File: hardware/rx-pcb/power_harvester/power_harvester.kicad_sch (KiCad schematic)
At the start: 30 parts, among them J1 Conn_Coaxial_Small, J2 Conn_01x02_Pin

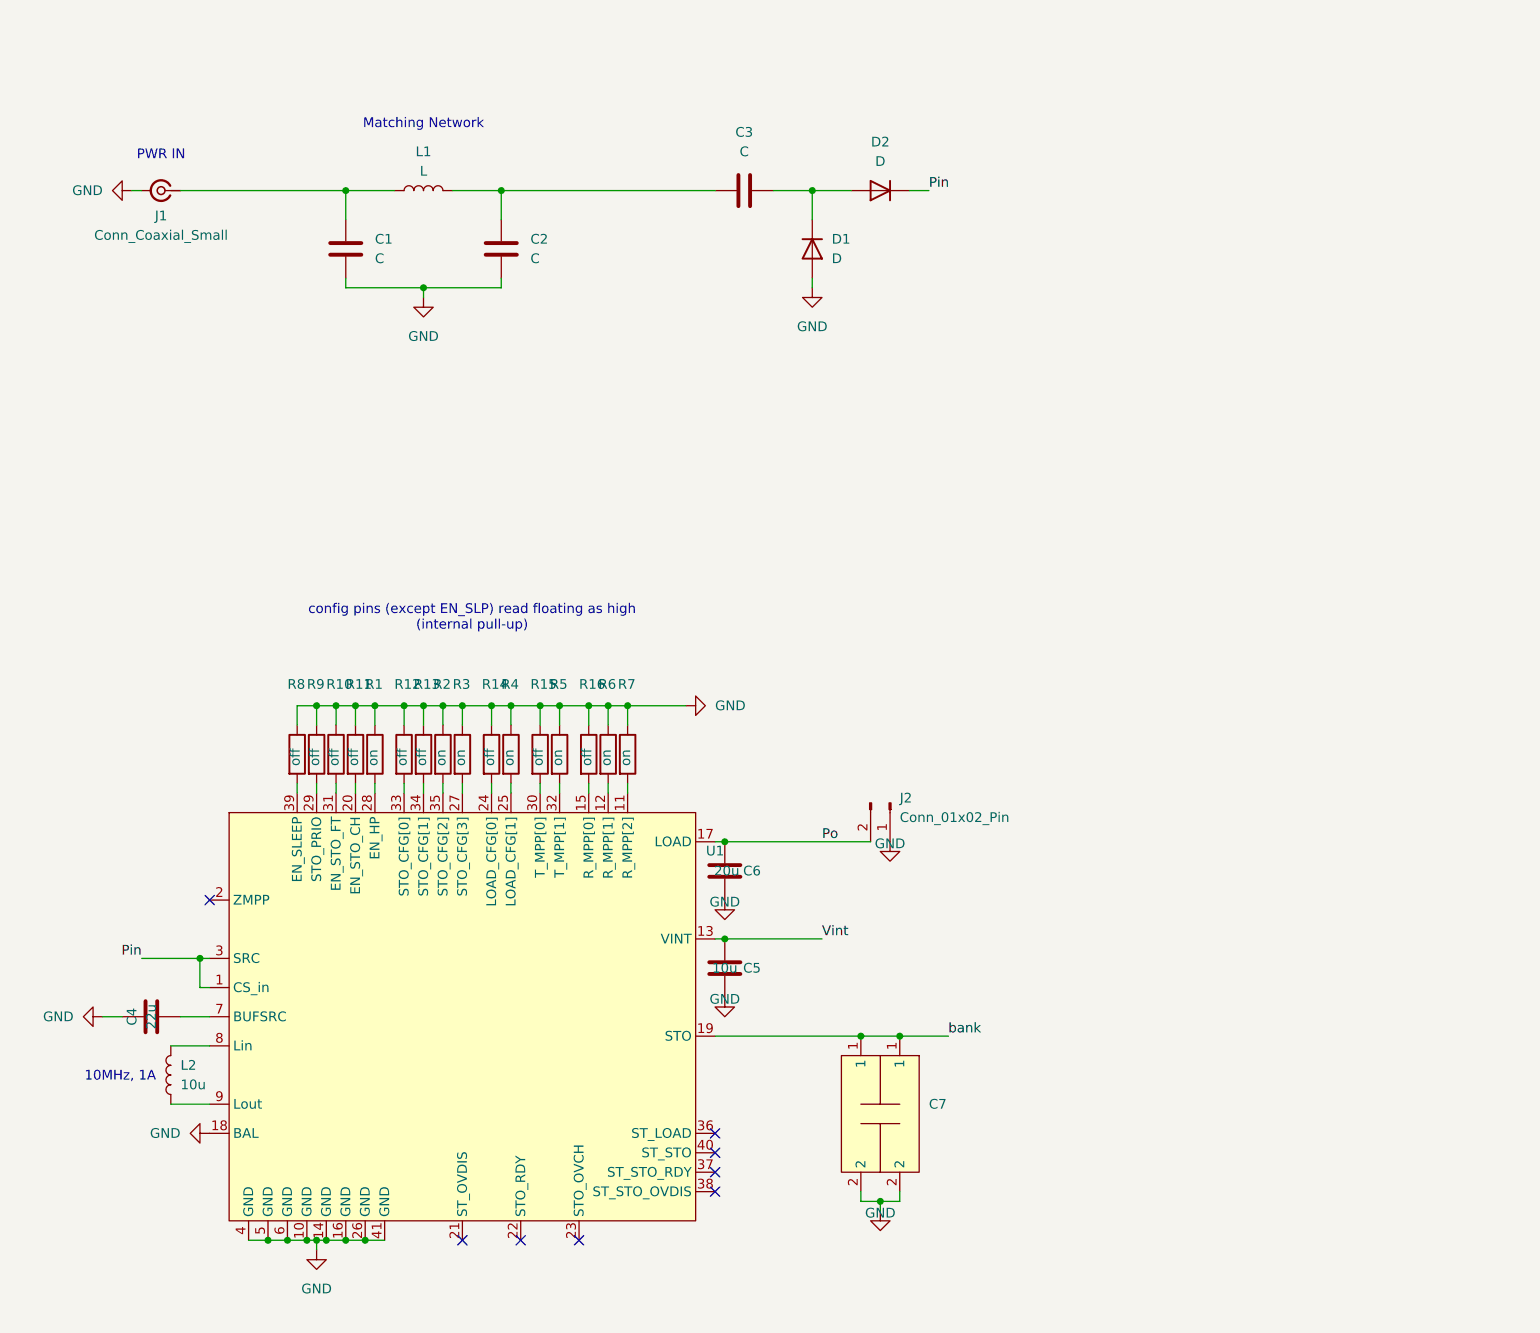
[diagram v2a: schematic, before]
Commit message: updated harvester PCB with reverse voltage suppression diodes.
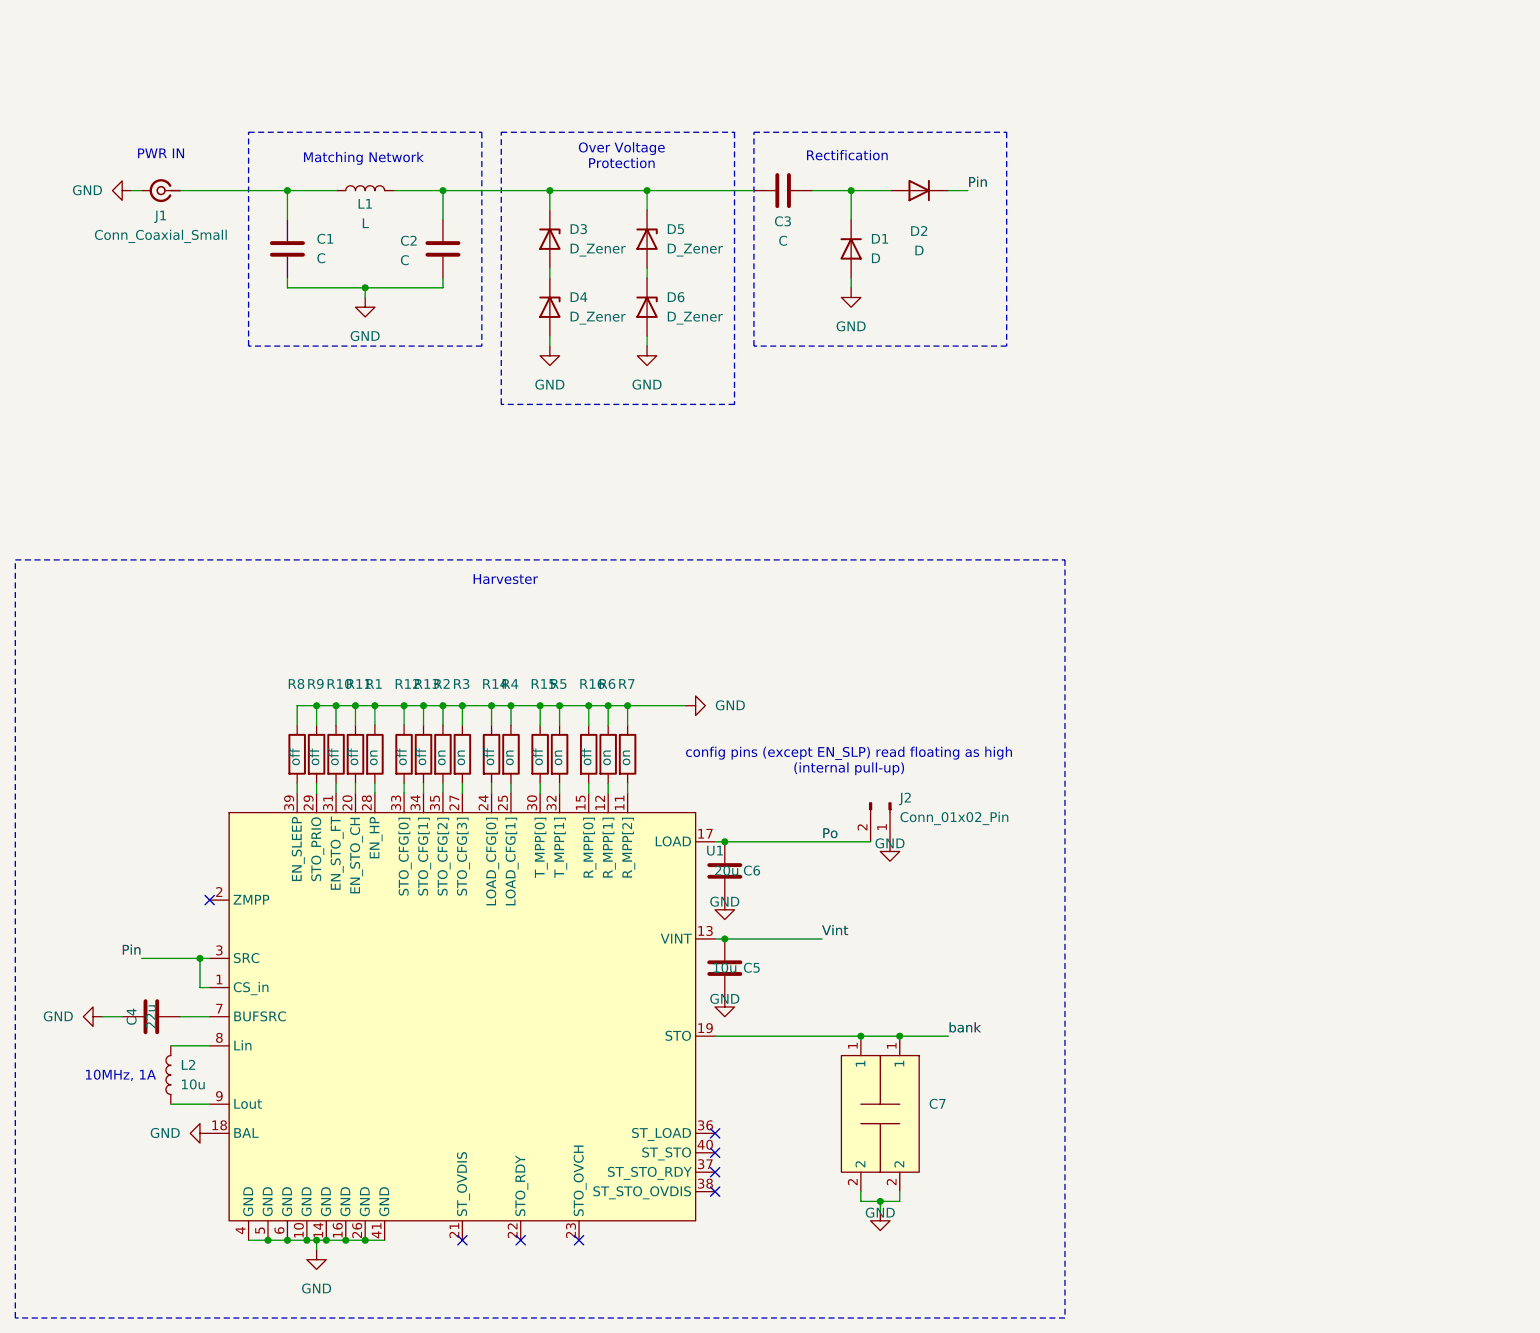
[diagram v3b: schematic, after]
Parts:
- added D3, D4, D5, D6: D_Zener, Capacitor_SMD:C_0201_0603Metric, symbol Device:D_Zener
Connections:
- net GND: now also D4.2 (A), D6.2 (A)
- net at C2.1, C3.1, L1.2: now also D3.1 (K), D5.1 (K)
- new net: D5.2 (A), D6.1 (K)
- new net: D3.2 (A), D4.1 (K)
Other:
- note added: "Harvester"
- note added: "Over Voltage Protection"
- note added: "Rectification"
- moved on the sheet: C1, C2, C3, D1, D2, L1

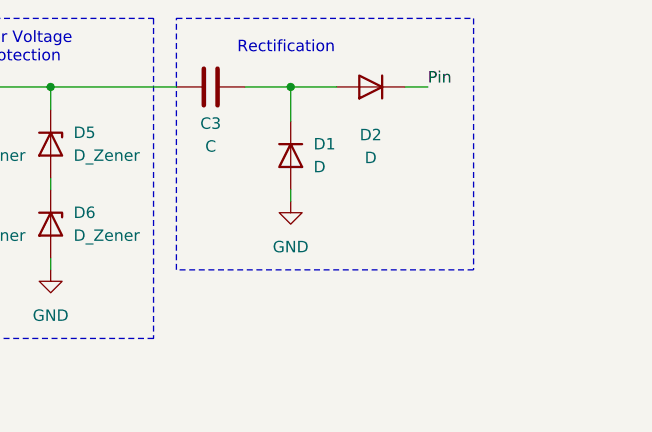
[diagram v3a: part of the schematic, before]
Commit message: updated harvester with compartmentalization testing resistors and test points. updated bluetooth test to use a low Vf diode rather than an LED for reverse current protection. must update footprint for that.
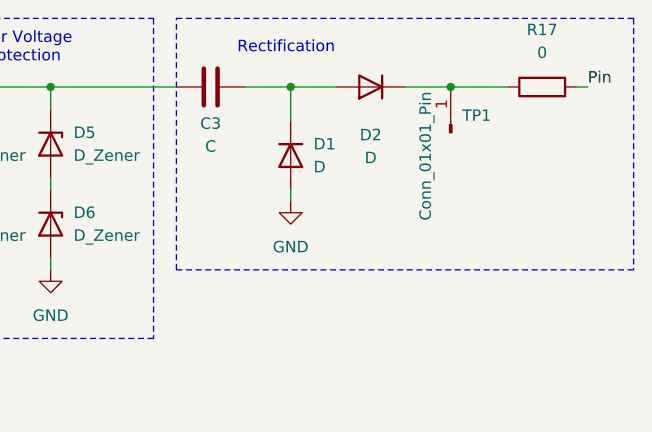
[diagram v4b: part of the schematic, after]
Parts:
- added R17: 0, Resistor_SMD:R_0201_0603Metric_Pad0.64x0.40mm_HandSolder, symbol Device:R
- added TP1: Conn_01x01_Pin, Connector_PinHeader_2.54mm:PinHeader_1x01_P2.54mm_Vertical, symbol Connector:Conn_01x01_Pin
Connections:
- net Pin: now also R17.2; no longer D2.1 (K)
- new net: D2.1 (K), R17.1, TP1.1 (Pin_1)
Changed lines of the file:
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@@
 	(rectangle
 		(start 109.22 38.1)
-		(end 142.24 66.04)
+		(end 160.02 66.04)
 		(stroke
 			(width 0)
@@
 		(color 0 0 0 0)
 	)
+	(junction
+		(at 139.7 45.72)
+		(diameter 0)
+		(color 0 0 0 0)
+	)
 	(no_connect
 		(at 86.36 182.88)
@@
 	(wire
 		(pts
+			(xy 134.62 45.72) (xy 139.7 45.72)
+		)
+		(stroke
+			(width 0)
+			(type default)
+		)
+	)
+	(wire
+		(pts
 			(xy 121.92 45.72) (xy 121.92 49.53)
 		)
@@
 	(wire
 		(pts
-			(xy 137.16 45.72) (xy 134.62 45.72)
+			(xy 146.05 45.72) (xy 139.7 45.72)
+		)
+		(stroke
+			(width 0)
+			(type default)
+		)
+	)
+	(wire
+		(pts
+			(xy 153.67 45.72) (xy 154.94 45.72)
 		)
 		(stroke
@@
 	)
 	(label "Pin"
-		(at 137.16 45.72 0)
+		(at 154.94 45.72 0)
 		(effects
 			(font
@@
 	)
 	(symbol
+		(lib_id "Device:R")
+		(at 149.86 45.72 90)
+		(unit 1)
+		(exclude_from_sim no)
+		(in_bom yes)
+		(on_board yes)
+		(dnp no)
+		(fields_autoplaced yes)
+		(property "Reference" "R17"
+			(at 149.86 39.37 90)
+			(effects
+				(font
+					(size 1.27 1.27)
+				)
+			)
+		)
+		(property "Value" "0"
+			(at 149.86 41.91 90)
+			(effects
+				(font
+					(size 1.27 1.27)
+				)
+			)
+		)
+		(property "Footprint" "Resistor_SMD:R_0201_0603Metric_Pad0.64x0.40mm_HandSolder"
+			(at 149.86 47.498 90)
+			(effects
+				(font
+					(size 1.27 1.27)
+				)
+				(hide yes)
+			)
+		)
+		(property "Datasheet" "~"
+			(at 149.86 45.72 0)
+			(effects
+				(font
+					(size 1.27 1.27)
+				)
+				(hide yes)
+			)
+		)
+		(property "Description" "Resistor"
+			(at 149.86 45.72 0)
+			(effects
+				(font
+					(size 1.27 1.27)
+				)
+				(hide yes)
+			)
+		)
+		(pin "1"
+		)
+		(pin "2"
+		)
+		(instances
+			(project ""
+				(path "/5e0abde9-f038-4a18-8052-8202be093003"
+					(reference "R17")
+					(unit 1)
+				)
+			)
+		)
+	)
+	(symbol
 		(lib_id "Connector:Conn_01x02_Pin")
 		(at 127 125.73 270)
@@
 					(unit 1)
 				)
+			)
+		)
+	)
+	(symbol
+		(lib_id "Connector:Conn_01x01_Pin")
+		(at 139.7 50.8 90)
+		(unit 1)
+		(exclude_from_sim no)
+		(in_bom yes)
+		(on_board yes)
+		(dnp no)
+		(property "Reference" "TP1"
+			(at 140.97 48.8949 90)
+			(effects
+				(font
+					(size 1.27 1.27)
+				)
+				(justify right)
+			)
+		)
+		(property "Value" "Conn_01x01_Pin"
+			(at 136.906 46.228 0)
+			(effects
+				(font
+					(size 1.27 1.27)
+				)
+				(justify right)
+			)
+		)
+		(property "Footprint" "Connector_PinHeader_2.54mm:PinHeader_1x01_P2.54mm_Vertical"
+			(at 139.7 50.8 0)
+			(effects
+				(font
+					(size 1.27 1.27)
+				)
+				(hide yes)
+			)
+		)
+		(property "Datasheet" "~"
+			(at 139.7 50.8 0)
+			(effects
+				(font
+					(size 1.27 1.27)
+				)
+				(hide yes)
+			)
+		)
+		(property "Description" "Generic connector, single row, 01x01, script generated"
+			(at 139.7 50.8 0)
+			(effects
+				(font
+					(size 1.27 1.27)
+				)
+				(hide yes)
+			)
+		)
+		(pin "1"
+		)
+		(instances
+			(project ""
+				(path "/5e0abde9-f038-4a18-8052-8202be093003"
+					(reference "TP1")
+					(unit 1)
+				)

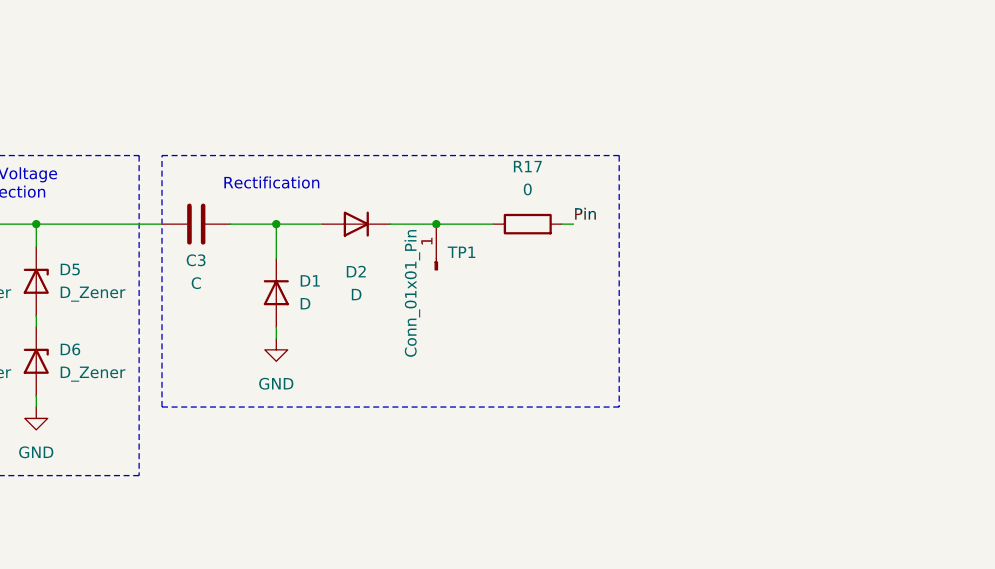
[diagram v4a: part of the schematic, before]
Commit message: simulation and cleaning
actually simulated my stupid 5k impedance match idea, it sucked because my rectifier is a 400 ohm impedance to ground. cleaning up the github.
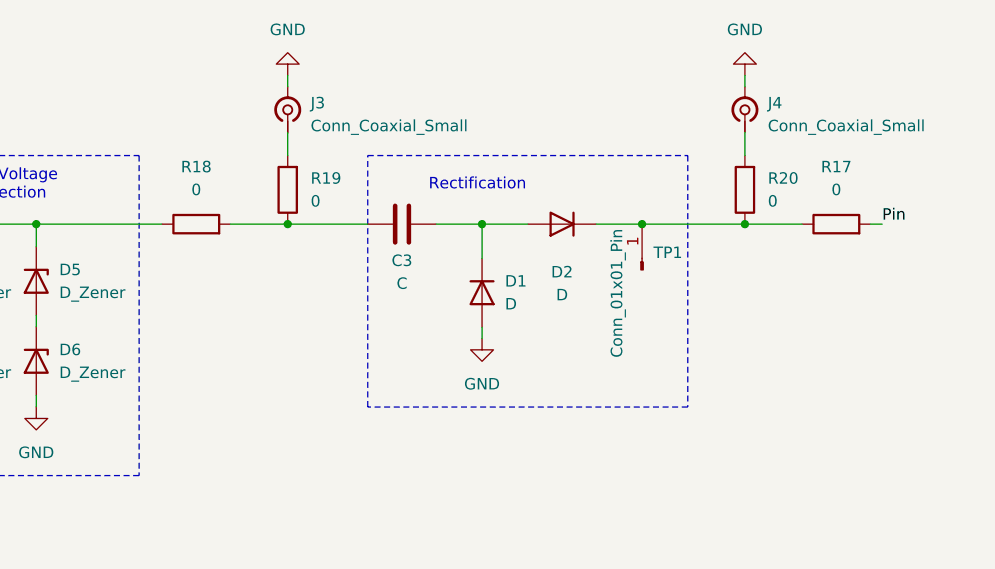
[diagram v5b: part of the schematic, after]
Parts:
- added J3, J4: Conn_Coaxial_Small, symbol Connector:Conn_Coaxial_Small
- added R18, R19, R20: 0, Resistor_SMD:R_0201_0603Metric_Pad0.64x0.40mm_HandSolder, symbol Device:R
- C7, U1: value ~ -> (none)
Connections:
- net GND: now also J3.2 (Ext), J4.2 (Ext)
- net at C2.1, D3.1 (K), D5.1 (K)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: now also R18.1; no longer C3.1
- net at D2.1 (K), R17.1, TP1.1 (Pin_1): now also R20.1
- new net: C3.1, R18.2, R19.1
- new net: J3.1 (In), R19.2
- new net: J4.1 (In), R20.2
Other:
- moved on the sheet: C3, D1, D2, R17, TP1

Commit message: power harvester updates and cleanup
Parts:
- removed D5, D6: D_Zener, Capacitor_SMD:C_0201_0603Metric, symbol Device:D_Zener
- removed TP1: Conn_01x01_Pin, Connector_PinHeader_2.54mm:PinHeader_1x01_P2.54mm_Vertical, symbol Connector:Conn_01x01_Pin
- added C10, C9: C, Capacitor_SMD:C_0603_1608Metric_Pad1.08x0.95mm_HandSolder, symbol Device:C
- added C8: 22u, Capacitor_SMD:C_0603_1608Metric_Pad1.08x0.95mm_HandSolder, symbol Device:C
- added L3: L, Inductor_SMD:L_0805_2012Metric_Pad1.05x1.20mm_HandSolder, symbol Device:L
- C1, C2, C4, C5, C6: footprint Capacitor_SMD:C_0805_2012Metric_Pad1.18x1.45mm_HandSolder -> Capacitor_SMD:C_0603_1608Metric_Pad1.08x0.95mm_HandSolder
- C3: value C -> 1n; footprint Capacitor_SMD:C_0805_2012Metric_Pad1.18x1.45mm_HandSolder -> Capacitor_SMD:C_0603_1608Metric_Pad1.08x0.95mm_HandSolder
- J3, J4: footprint (none) -> Connector_PinHeader_2.54mm:PinHeader_1x02_P2.54mm_Vertical
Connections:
- net GND: now also C10.2, C8.1, C9.2; no longer C1.2, C2.2
- net at D2.1 (K), R17.1, R20.1: now also C8.2
- net at C2.1, D3.1 (K), R18.1: now also L1.1, L3.2; no longer L1.2
- net at C1.1, J1.1 (In): now also L1.2, L3.1; no longer L1.1
- new net: C10.1, C2.2
- new net: C1.2, C9.1
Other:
- moved on the sheet: D3, D4, J4, L1, R17, R20

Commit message: harvester updates
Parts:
- added R21, R22, R23, R24, R25: x, Resistor_SMD:R_0805_2012Metric_Pad1.20x1.40mm_HandSolder, symbol Device:R
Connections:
- net GND: now also R24.2
- net Pin: now also R25.2
- net bank: now also R21.1
- net at U1.2 (ZMPP): now also R25.1
- net at U1.21 (ST_OVDIS): now also R21.2, R22.1
- net at U1.22 (STO_RDY): now also R22.2, R23.1
- net at U1.23 (STO_OVCH): now also R23.2, R24.1
- no-connect marks 8 -> 4
